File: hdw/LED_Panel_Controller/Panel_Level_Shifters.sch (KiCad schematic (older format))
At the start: 68 parts

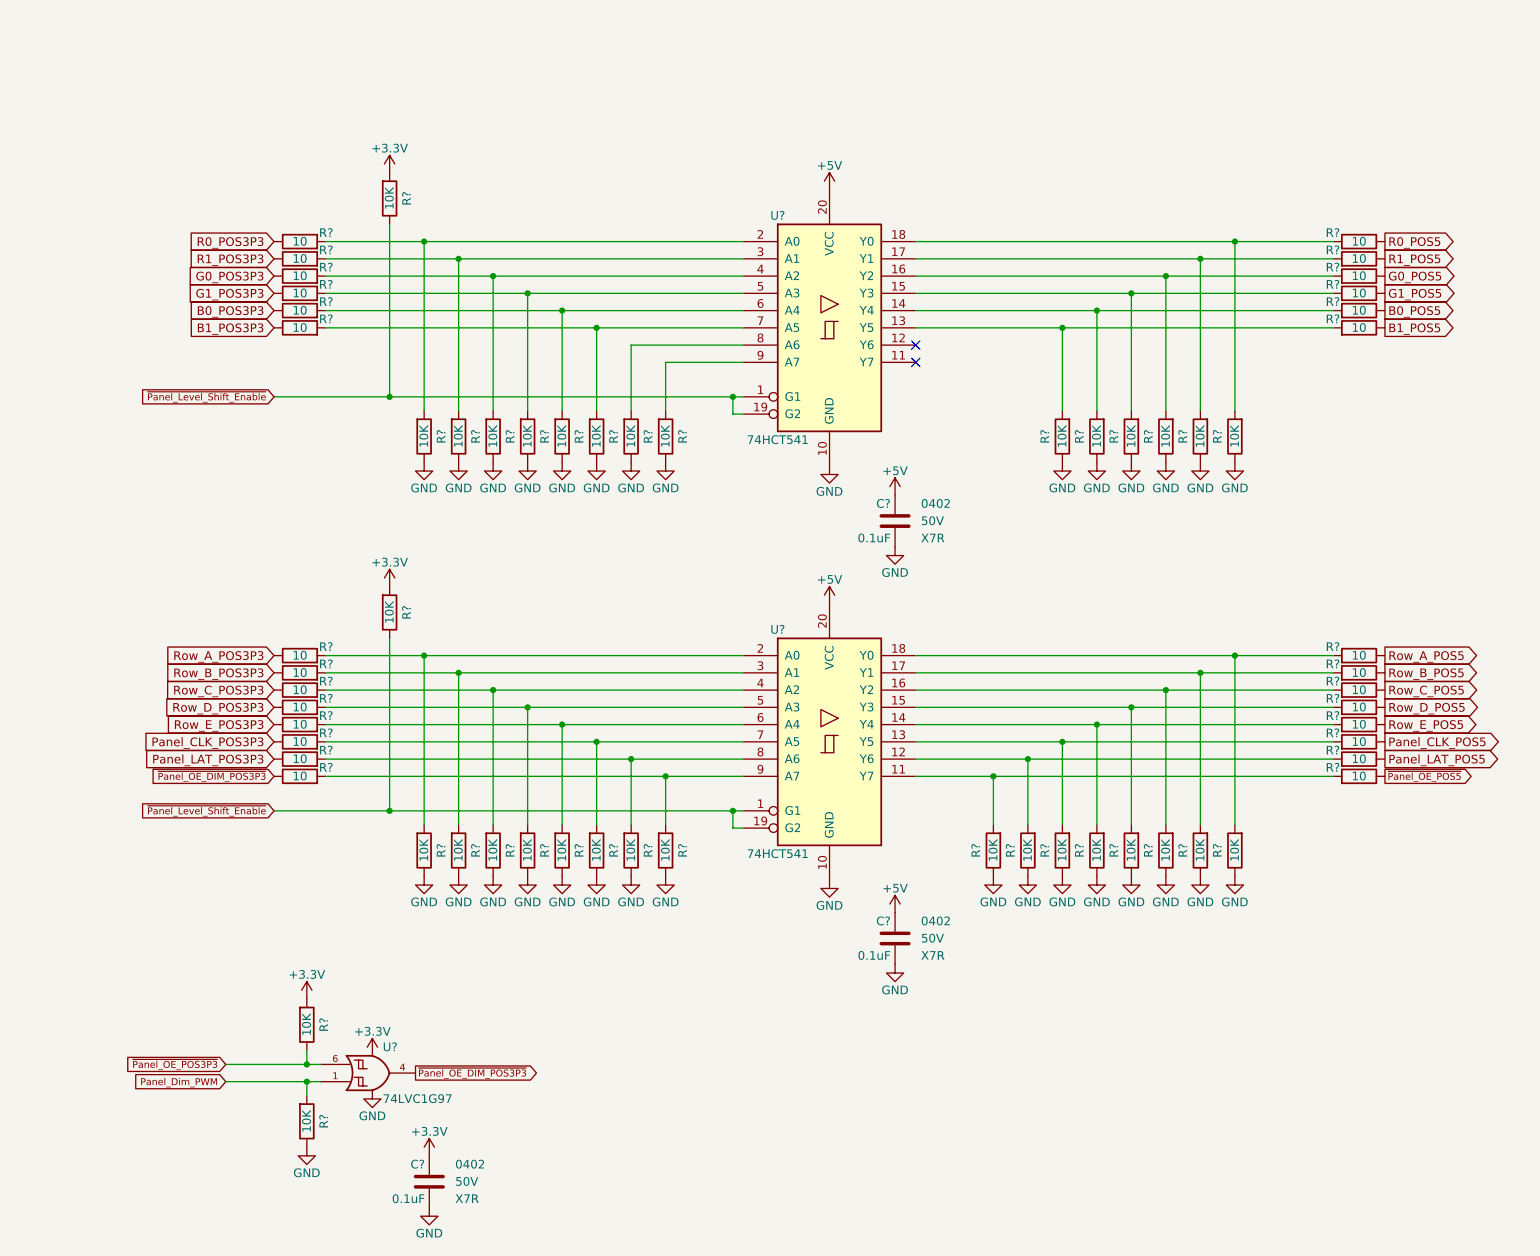
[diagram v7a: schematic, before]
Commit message: assigned I2C addresses
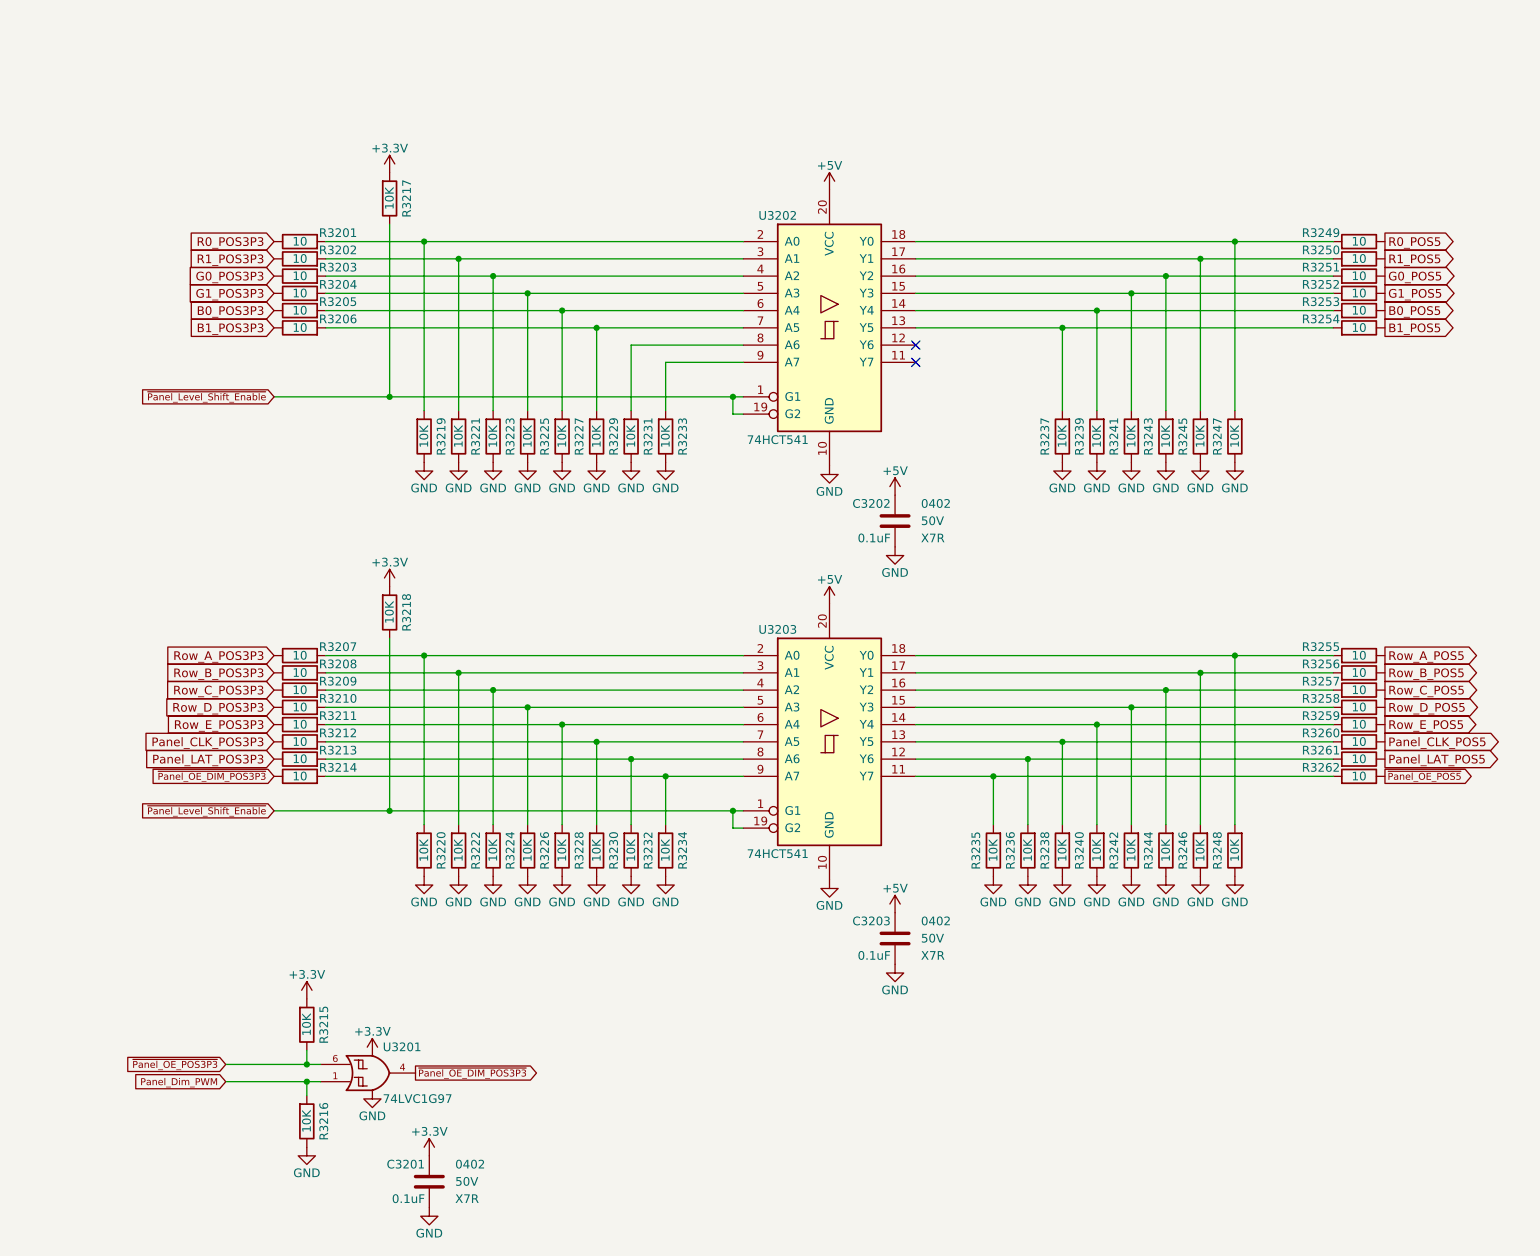
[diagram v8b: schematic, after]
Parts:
- gave numbers to parts that had none: 68
